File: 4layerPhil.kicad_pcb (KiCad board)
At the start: 4 copper layers, 71 x 54 mm, 54 parts, among them J1 USB_C_Receptacle_USB2.0_16P, J2 Conn_01x05_Pin, J3 Conn_01x04_Pin, J5 Conn_01x06_Pin, J6 1140084168, SW1 SW_SPDT, SW2 BTN1, SW3 BTN2, SW4 BTN3, U1 AMS1117-3.3, U2 USBLC6-2SC6, U3 STM32F103RCTx, Y1 16MHz

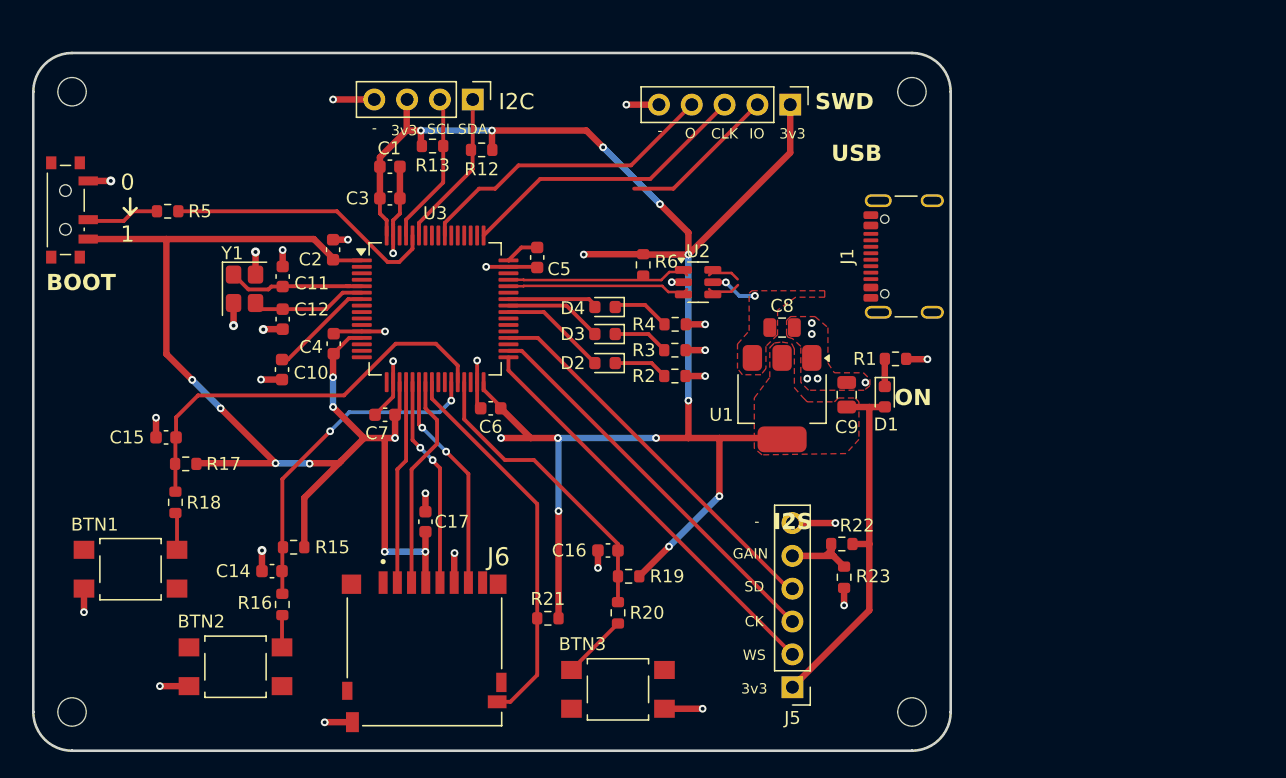
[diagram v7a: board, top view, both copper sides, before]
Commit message: Created power supply circuit for new regulator, deleted ancient AMS1117
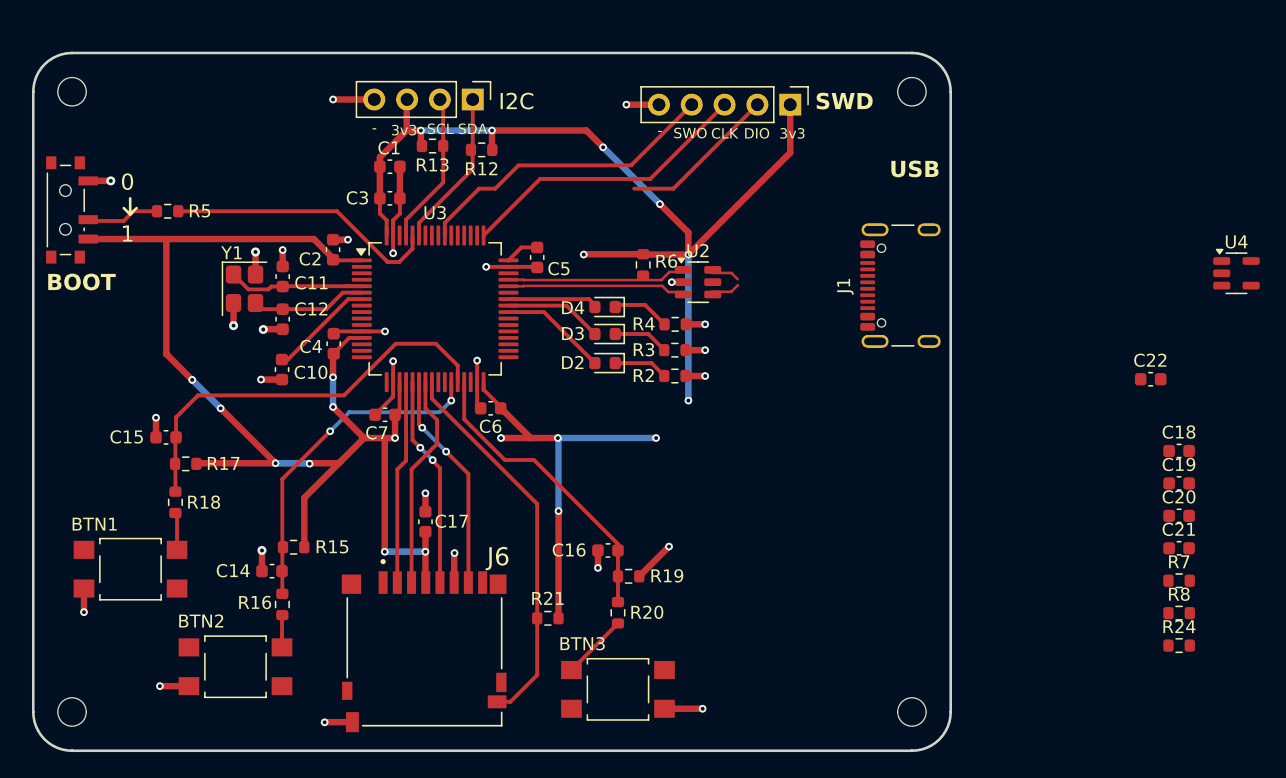
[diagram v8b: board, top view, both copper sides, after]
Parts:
- removed C8, C9: 22u, Capacitor_SMD:C_0805_2012Metric
- removed D1: RED, LED_SMD:LED_0603_1608Metric
- removed J5: Conn_01x06_Pin, Connector_PinHeader_2.54mm:PinHeader_1x06_P2.54mm_Vertical
- removed R1: 1k5, Resistor_SMD:R_0603_1608Metric
- removed R22, R23: 100k, Resistor_SMD:R_0603_1608Metric
- removed U1: AMS1117-3.3, Package_TO_SOT_SMD:SOT-223-3_TabPin2
- added C18: 470n, Capacitor_SMD:C_0603_1608Metric, F.Cu at (195.7, 84.8)
- added C19: 470n, Capacitor_SMD:C_0603_1608Metric, F.Cu at (195.7, 87.3)
- added C20: 10u, Capacitor_SMD:C_0603_1608Metric, F.Cu at (195.7, 89.8)
- added C21: 470n, Capacitor_SMD:C_0603_1608Metric, F.Cu at (195.7, 92.3)
- added C22: 10u, Capacitor_SMD:C_0603_1608Metric, F.Cu at (193.5, 79.2)
- added R24: 0, Resistor_SMD:R_0603_1608Metric, F.Cu at (195.7, 99.9)
- added R7: 5.1k, Resistor_SMD:R_0603_1608Metric, F.Cu at (195.7, 94.8)
- added R8: 5.1k, Resistor_SMD:R_0603_1608Metric, F.Cu at (195.7, 97.4)
- added U4: SPX3819M5-L-3-3, Package_TO_SOT_SMD:SOT-23-5, F.Cu at (200.1, 71.0)
- moved J1 2.26 mm to (175.2, 72.0)
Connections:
- J1 pad A5: unconnected-(J1-CC1-PadA5) -> /USBCC1
- J1 pad B5: unconnected-(J1-CC2-PadB5) -> /USBCC2
- U3 pad 33: /I2S2_WS -> unconnected-(U3-PB12-Pad33)
- U3 pad 34: /I2S2_CK -> unconnected-(U3-PB13-Pad34)
- U3 pad 36: /I2S2_SD -> unconnected-(U3-PB15-Pad36)
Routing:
- net +3V3: track 270.0 -> 218.9 mm, vias 22 -> 21
- net /I2S2_WS: track 32.1 -> 0.00 mm
- net /I2S2_CK: track 30.7 -> 0.00 mm
- net /I2S2_SD: track 30.0 -> 0.00 mm
- net /I2S2_GAIN: track 6.43 -> 0.00 mm
- net GND: track 69.1 -> 62.8 mm, vias 35 -> 27
- net VBUS: track 3.92 -> 0.00 mm, vias 2 -> 0
- net /PWR_LED_K: track 2.14 -> 0.00 mm
- removed copper zone on F.Cu, net +3V3
- removed copper zone on F.Cu, net GND
- removed copper zone on F.Cu, net VBUS
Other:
- board text added: "DIO"
- board text added: "SWO"
- board text removed: "CK"
- board text removed: "GAIN"
- board text removed: "I2S"
- board text removed: "IO"
- board text removed: "O"
- board text removed: "ON"
- board text removed: "SD"
- board text removed: "WS"
